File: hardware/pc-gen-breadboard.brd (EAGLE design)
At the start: 43.2 x 30.5 mm, 25 parts

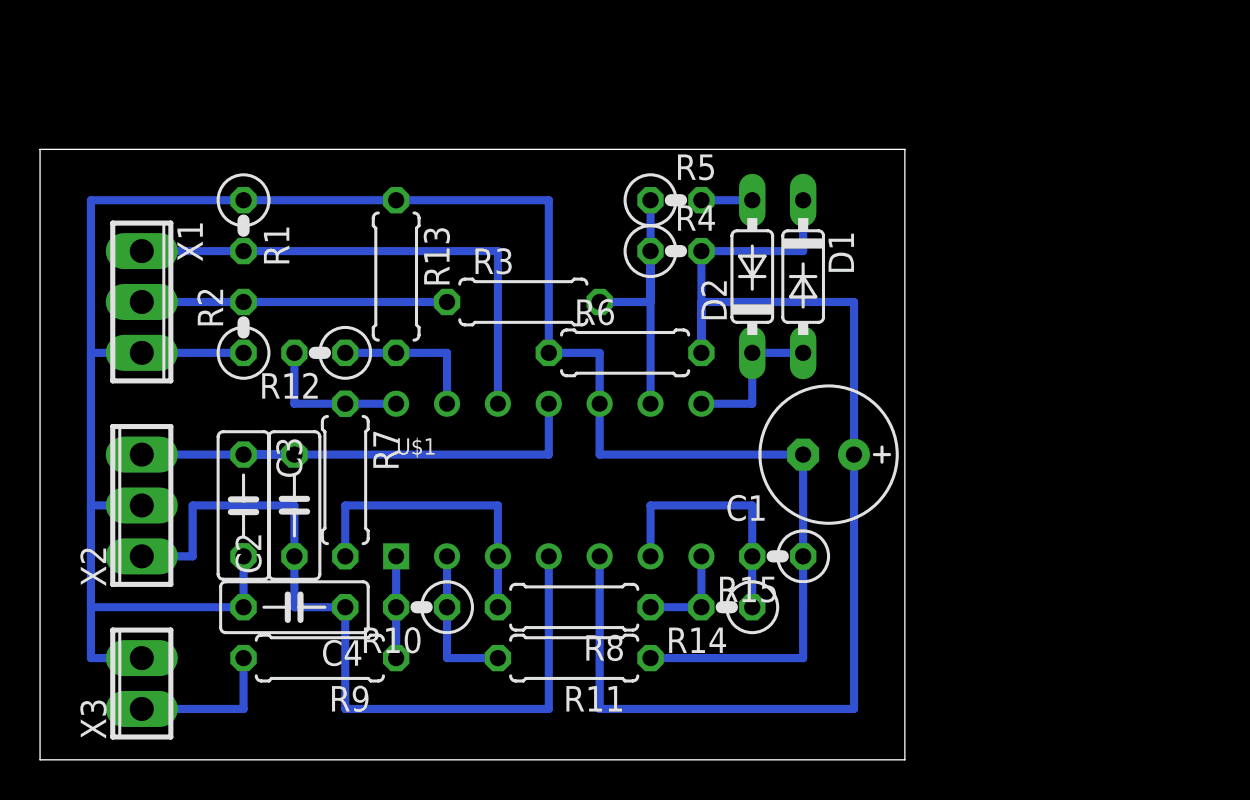
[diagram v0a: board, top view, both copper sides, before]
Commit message: gain selector added
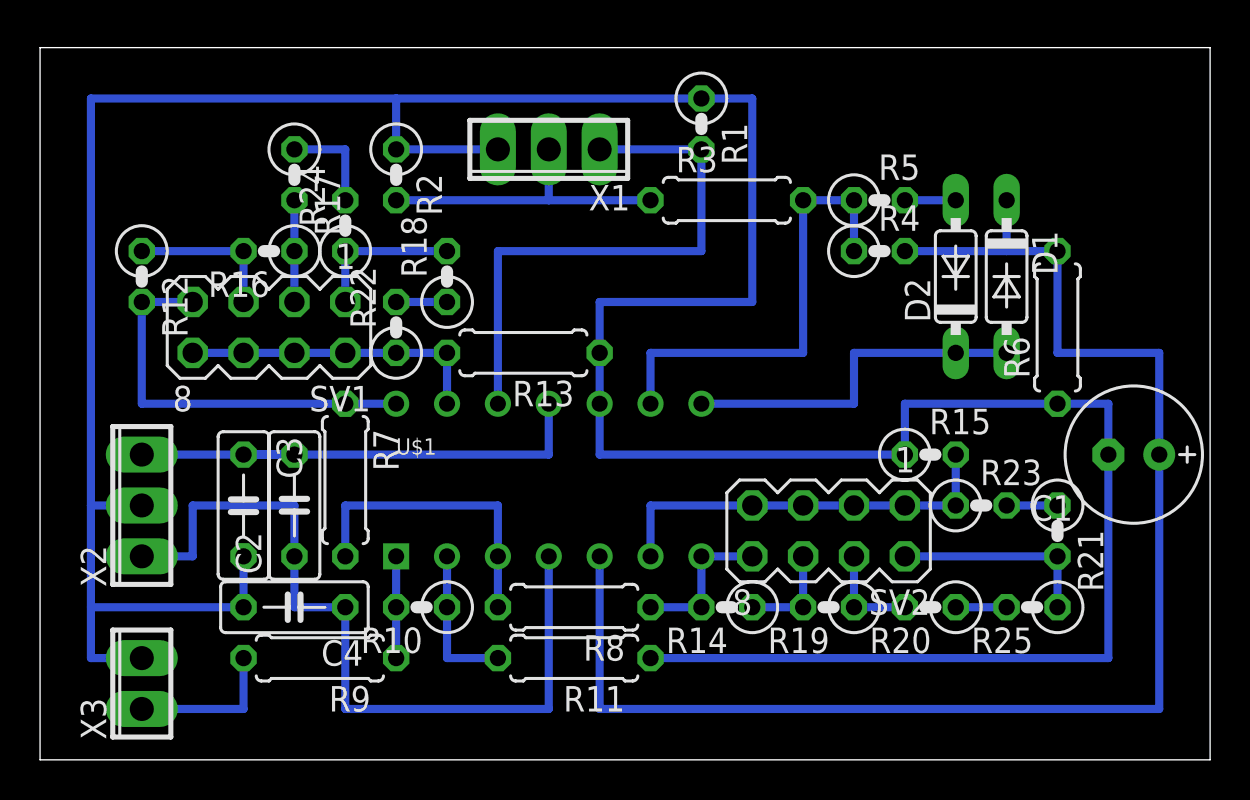
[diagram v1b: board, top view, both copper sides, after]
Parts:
- added R16, R19: 200k, rcl:0207/2V
- added R17, R20: 390k, rcl:0207/2V
- added R18, R21: 750k, rcl:0207/2V
- added R22, R23: 51k, rcl:0207/2V
- added R24, R25: 10k, rcl:0207/2V
- added SV1, SV2: (no value), con-lstb:MA04-2
- C1: value (none) -> 1u
- R6: value (none) -> 1k
- moved R1 23.4 mm to (33.0, 31.8)
- moved X1 21.7 mm to (25.4, 30.5), turned to 180 degrees
- moved R6 21.6 mm to (50.8, 21.6), turned to 90 degrees
- moved C1 15.2 mm to (54.6, 15.2)
- moved R3 11.4 mm to (34.3, 27.9)
- moved R2 10.8 mm to (17.8, 29.2), turned to 270 degrees
- moved D1 10.2 mm to (48.3, 24.1)
- moved D2 10.2 mm to (45.7, 24.1)
- moved R4 10.2 mm to (41.9, 25.4)
- moved R5 10.2 mm to (41.9, 27.9)
- moved R12 9.67 mm to (5.08, 24.1), turned to 270 degrees
- moved R15 9.16 mm to (44.5, 15.2), turned to 0 degrees
- moved R13 7.41 mm to (24.1, 20.3), turned to 180 degrees
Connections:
- new net N$17: R12.1, R16.2, SV1.5
- new net N$18: R16.1, R17.2, SV1.3
- new net N$19: R18.2, R24.1, SV1.1
- new net N$20: R14.1, R19.2, SV2.6
- new net N$21: R18.1, R22.2
- new net N$22: R13.2, R22.1, SV1.2, SV1.4, SV1.6, SV1.8, U$1.13
- new net N$23: R19.1, R20.2, SV2.4
- new net N$24: R17.1, R24.2
- new net N$25: R21.1, R23.2
- new net N$26: R20.1, R25.2
- net N$10: now also R23.1, SV2.1, SV2.3, SV2.5, SV2.7; no longer R14.1
- net N$12: now also SV2.8
- net N$5: now also R21.2, R25.1, SV2.2; no longer R12.1, R13.2, U$1.13
- net N$8: now also SV1.7
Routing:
- net GND: track 111.8 -> 172.7 mm
- net N$22: track 0.00 -> 15.2 mm
- net N$8: track 7.62 -> 20.3 mm
- net N$11: track 63.5 -> 73.7 mm
- net N$9: track 7.62 -> 17.8 mm
- net N$6: track 15.2 -> 22.9 mm
- net N$10: track 12.7 -> 20.3 mm
- net N$19: track 0.00 -> 7.62 mm
- net N$17: track 0.00 -> 7.62 mm
- net N$18: track 0.00 -> 5.08 mm
- net N$24: track 0.00 -> 5.08 mm
- net N$23: track 0.00 -> 5.08 mm
- net N$20: track 0.00 -> 5.08 mm
- net N$4: track 25.4 -> 27.9 mm
- net N$26: track 0.00 -> 2.54 mm
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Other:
- board size 43.2 x 30.5 mm -> 58.4 x 35.6 mm

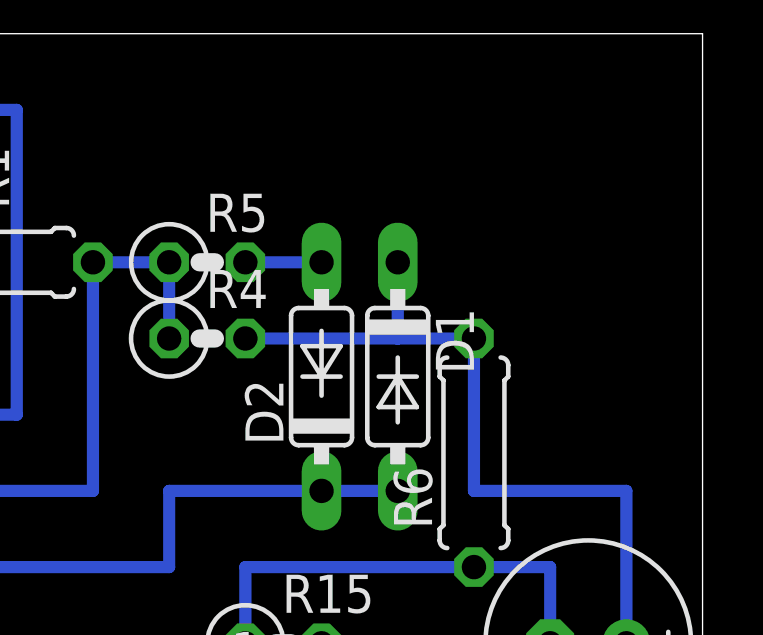
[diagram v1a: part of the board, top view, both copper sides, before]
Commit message: offest polarity selector added
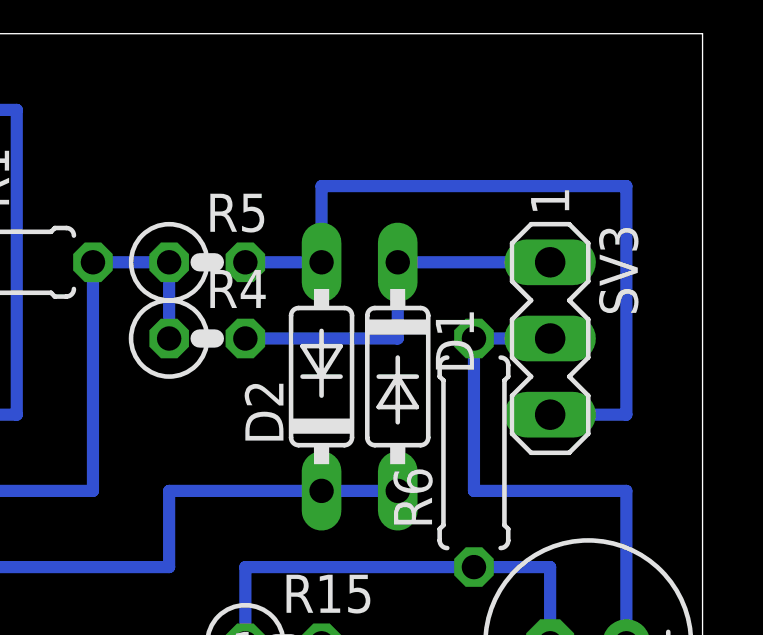
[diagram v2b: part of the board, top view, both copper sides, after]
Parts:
- added SV3: (no value), con-lstb:MA03-1
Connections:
- new net N$27: C1.+, R6.2, SV3.2, U$1.5
- net N$11: now also SV3.1; no longer C1.+, R6.2, U$1.5
- net N$7: now also SV3.3
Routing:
- net N$27: track 0.00 -> 66.0 mm
- net N$11: track 73.7 -> 12.7 mm
- net N$7: track 2.54 -> 25.4 mm
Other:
- board text added: "+"
- board text added: "-"
- board text added: "Polarity"
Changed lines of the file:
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@@
 <wire x1="58.42" y1="35.56" x2="0" y2="35.56" width="0" layer="20"/>
 <wire x1="0" y1="35.56" x2="0" y2="0" width="0" layer="20"/>
-<text x="-10.16" y="22.86" size="2.54" layer="49">In</text>
+<text x="22.86" y="40.64" size="2.54" layer="49">In</text>
 <text x="-10.16" y="2.54" size="2.54" layer="49">Out</text>
 <text x="-15.24" y="12.7" size="2.54" layer="49">Supply</text>
-<text x="-4.318" y="19.558" size="1.27" layer="49">GND</text>
-<text x="-4.318" y="22.098" size="1.27" layer="49">Offset</text>
-<text x="-4.318" y="24.892" size="1.27" layer="49">Signal</text>
+<text x="23.622" y="33.782" size="1.27" layer="49" rot="R90">GND</text>
+<text x="26.162" y="33.782" size="1.27" layer="49" rot="R90">Offset</text>
+<text x="28.448" y="33.782" size="1.27" layer="49" rot="R90">Signal</text>
 <text x="-3.81" y="12.192" size="1.27" layer="49">GND</text>
 <text x="-3.81" y="14.478" size="1.27" layer="49">+8V</text>
@@
 <text x="-4.064" y="4.572" size="1.27" layer="49">GND</text>
 <text x="-4.064" y="2.032" size="1.27" layer="49">Signal</text>
+<text x="60.96" y="24.13" size="2.54" layer="49">Polarity</text>
+<text x="59.182" y="25.908" size="1.27" layer="49">+</text>
+<text x="59.182" y="23.622" size="1.27" layer="49">-</text>
 </plain>
 <attributes>
@@
 <element name="R24" library="rcl" package="0207/2V" value="10k" x="15.24" y="26.67" rot="R90"/>
 <element name="R25" library="rcl" package="0207/2V" value="10k" x="49.53" y="7.62" rot="R180"/>
+<element name="SV3" library="con-lstb" package="MA03-1" value="" x="53.34" y="25.4" rot="R270">
+<attribute name="OC_NEWARK" value="unknown" x="53.34" y="25.4" size="1.27" layer="27" font="vector" ratio="20" rot="R270" display="off"/>
+<attribute name="MPN" value="" x="53.34" y="25.4" size="1.27" layer="27" font="vector" ratio="20" rot="R270" display="off"/>
+<attribute name="MF" value="" x="53.34" y="25.4" size="1.27" layer="27" font="vector" ratio="20" rot="R270" display="off"/>
+<attribute name="OC_FARNELL" value="unknown" x="53.34" y="25.4" size="1.27" layer="27" font="vector" ratio="20" rot="R270" display="off"/>
+</element>
 </elements>
 <signals>
@@
 <contactref element="D2" pad="A"/>
 <wire x1="43.18" y1="27.94" x2="45.72" y2="27.94" width="0.4064" layer="16"/>
+<contactref element="SV3" pad="3"/>
+<wire x1="53.34" y1="22.86" x2="55.88" y2="22.86" width="0.4064" layer="16"/>
+<wire x1="55.88" y1="22.86" x2="55.88" y2="30.48" width="0.4064" layer="16"/>
+<wire x1="55.88" y1="30.48" x2="45.72" y2="30.48" width="0.4064" layer="16"/>
+<wire x1="45.72" y1="30.48" x2="45.72" y2="27.94" width="0.4064" layer="16"/>
 </signal>
 <signal name="N$9">
@@
 </signal>
 <signal name="N$11">
+<contactref element="D1" pad="C"/>
+<wire x1="48.26" y1="27.94" x2="48.26" y2="25.4" width="0.4064" layer="16"/>
 <contactref element="R4" pad="2"/>
-<contactref element="D1" pad="C"/>
-<contactref element="C1" pad="+"/>
-<contactref element="R6" pad="2"/>
-<wire x1="48.26" y1="27.94" x2="48.26" y2="25.4" width="0.4064" layer="16"/>
-<wire x1="48.26" y1="25.4" x2="43.18" y2="25.4" width="0.4064" layer="16"/>
-<contactref element="U$1" pad="5"/>
-<wire x1="27.94" y1="10.16" x2="27.94" y2="2.54" width="0.4064" layer="16"/>
-<wire x1="27.94" y1="2.54" x2="55.88" y2="2.54" width="0.4064" layer="16"/>
-<wire x1="55.88" y1="2.54" x2="55.88" y2="15.24" width="0.4064" layer="16"/>
-<wire x1="55.88" y1="20.32" x2="55.88" y2="15.24" width="0.4064" layer="16"/>
-<wire x1="55.88" y1="20.32" x2="50.8" y2="20.32" width="0.4064" layer="16"/>
-<wire x1="50.8" y1="20.32" x2="50.8" y2="25.4" width="0.4064" layer="16"/>
-<wire x1="48.26" y1="25.4" x2="50.8" y2="25.4" width="0.4064" layer="16"/>
+<contactref element="SV3" pad="1"/>
+<wire x1="48.26" y1="27.94" x2="53.34" y2="27.94" width="0.4064" layer="16"/>
+<wire x1="43.18" y1="25.4" x2="48.26" y2="25.4" width="0.4064" layer="16"/>
 </signal>
 <signal name="N$12">
@@
 <wire x1="45.72" y1="7.62" x2="48.26" y2="7.62" width="0.4064" layer="16"/>
 </signal>
+<signal name="N$27">
+<contactref element="C1" pad="+"/>
+<contactref element="R6" pad="2"/>
+<contactref element="U$1" pad="5"/>
+<wire x1="27.94" y1="10.16" x2="27.94" y2="2.54" width="0.4064" layer="16"/>
+<wire x1="27.94" y1="2.54" x2="55.88" y2="2.54" width="0.4064" layer="16"/>
+<wire x1="55.88" y1="2.54" x2="55.88" y2="15.24" width="0.4064" layer="16"/>
+<wire x1="55.88" y1="20.32" x2="55.88" y2="15.24" width="0.4064" layer="16"/>
+<wire x1="55.88" y1="20.32" x2="50.8" y2="20.32" width="0.4064" layer="16"/>
+<wire x1="50.8" y1="20.32" x2="50.8" y2="25.4" width="0.4064" layer="16"/>
+<contactref element="SV3" pad="2"/>
+<wire x1="53.34" y1="25.4" x2="50.8" y2="25.4" width="0.4064" layer="16"/>
+</signal>
 </signals>

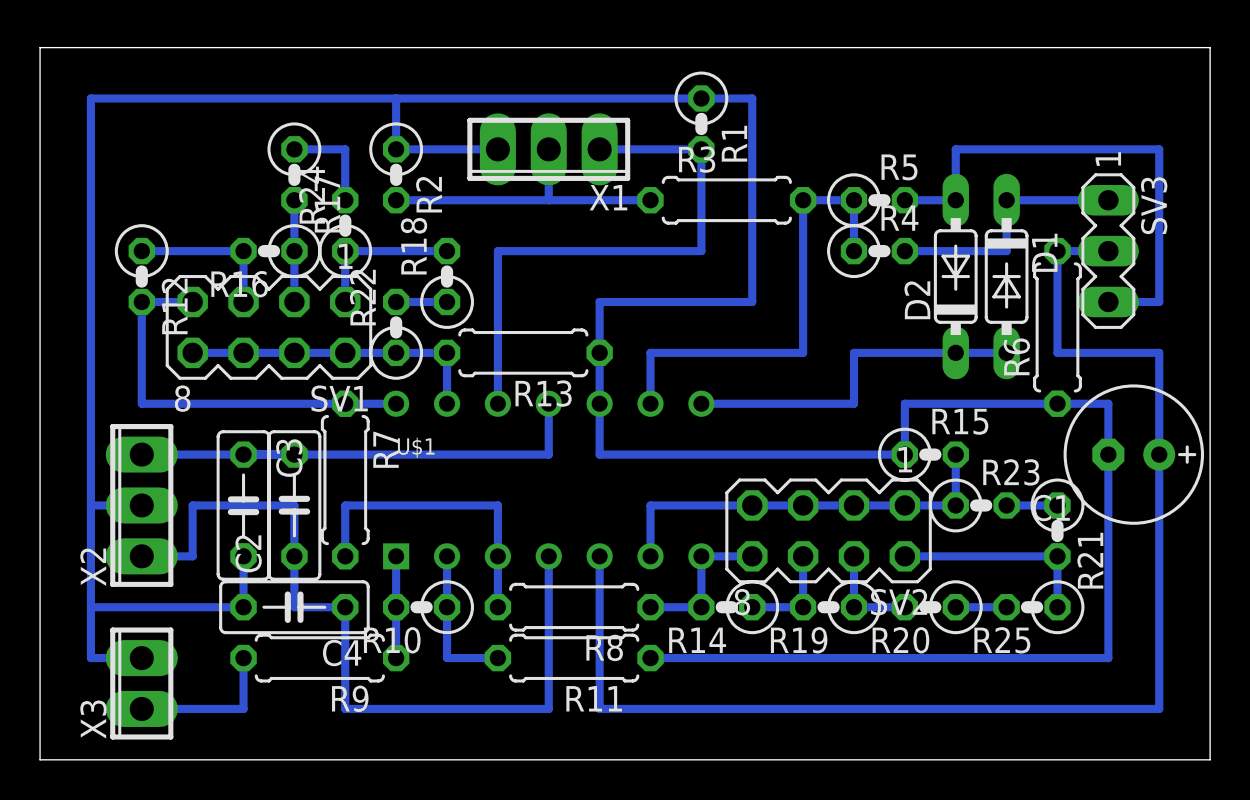
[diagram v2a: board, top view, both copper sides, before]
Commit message: small changes in layout to optimize pcb size
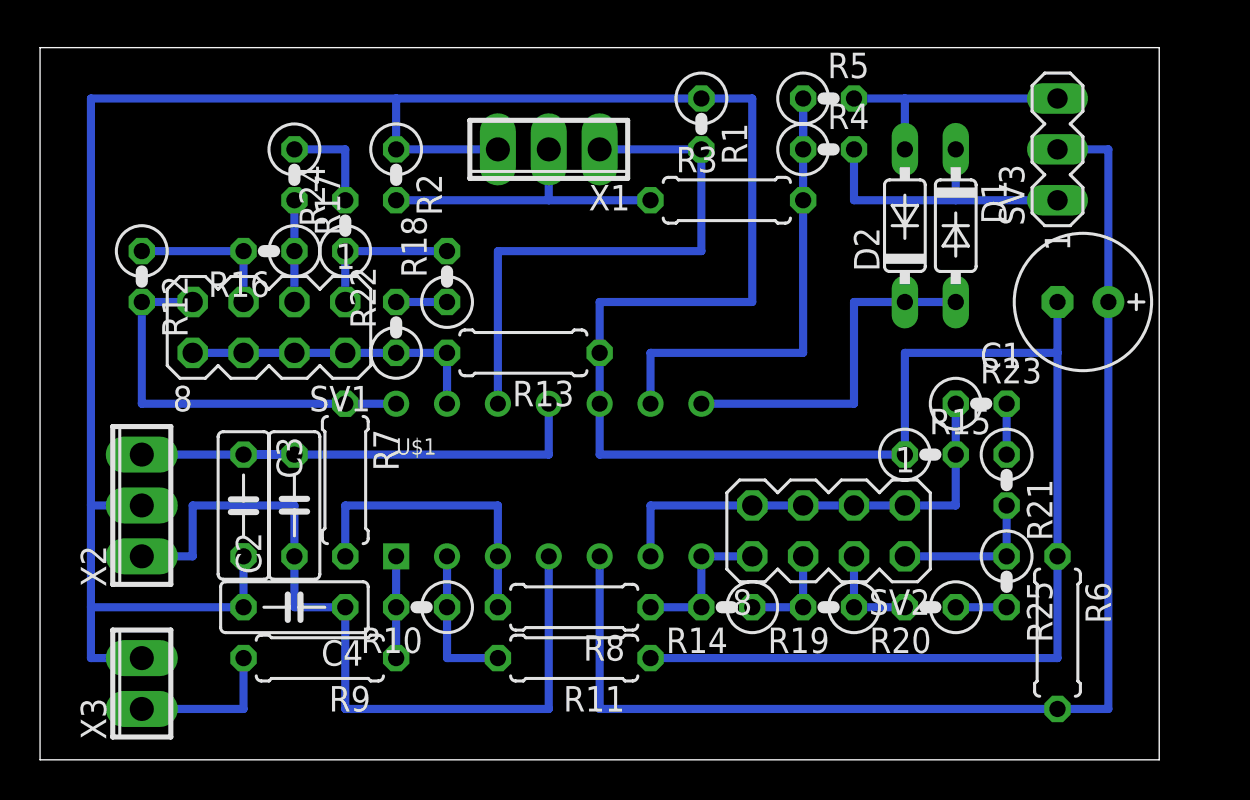
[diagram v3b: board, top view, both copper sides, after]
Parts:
- moved R6 15.2 mm to (50.8, 6.35), turned to 270 degrees
- moved C1 8.03 mm to (52.1, 22.9)
- moved SV3 5.68 mm to (50.8, 30.5), turned to 90 degrees
- moved R4 5.68 mm to (39.4, 30.5)
- moved R5 5.68 mm to (39.4, 33.0)
- moved R23 5.08 mm to (47.0, 17.8)
- moved D1 3.59 mm to (45.7, 26.7)
- moved D2 3.59 mm to (43.2, 26.7)
- moved R21 3.59 mm to (48.3, 14.0)
- moved R25 1.80 mm to (48.3, 8.89), turned to 270 degrees
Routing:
- net N$7: track 25.4 -> 12.7 mm
- net N$27: track 66.0 -> 63.5 mm
- net N$6: track 22.9 -> 25.4 mm
- net N$5: track 10.2 -> 7.62 mm
- net N$10: track 20.3 -> 22.9 mm
- net GND: track 172.7 -> 175.3 mm
- net N$11: track 12.7 -> 15.2 mm
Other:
- board size 58.4 x 35.6 mm -> 55.9 x 35.6 mm

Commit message: small changes in layout
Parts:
- R6: device rcl:0207/7 -> rcl:0207/2V
- moved R18 15.5 mm to (5.08, 26.7), turned to 270 degrees
- moved R22 14.5 mm to (6.35, 30.5), turned to 180 degrees
- moved D2 13.0 mm to (30.5, 29.2)
- moved R24 11.4 mm to (5.08, 21.6), turned to 270 degrees
- moved R3 11.4 mm to (24.1, 22.9)
- moved R1 10.9 mm to (24.1, 25.4), turned to 180 degrees
- moved R25 10.5 mm to (45.7, 19.1)
- moved R12 9.67 mm to (14.0, 20.3), turned to 0 degrees
- moved R14 9.67 mm to (43.2, 11.4), turned to 270 degrees
- moved R17 9.67 mm to (8.89, 20.3), turned to 0 degrees
- moved R15 9.16 mm to (36.8, 20.3)
- moved R23 9.16 mm to (39.4, 22.9)
- moved R21 9.16 mm to (43.2, 21.6)
- moved D1 8.98 mm to (36.8, 27.9), turned to 180 degrees
- moved R19 8.98 mm to (45.7, 14.0), turned to 270 degrees
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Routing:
- net GND: track 175.3 -> 162.6 mm
- net N$4: track 27.9 -> 15.2 mm
- net N$8: track 20.3 -> 7.62 mm
- net N$22: track 15.2 -> 25.4 mm
- net N$12: track 7.62 -> 17.8 mm
- net N$11: track 15.2 -> 7.62 mm
- net N$7: track 12.7 -> 17.8 mm
- net N$9: track 17.8 -> 12.7 mm
- net N$6: track 25.4 -> 30.5 mm
- net N$27: track 63.5 -> 61.0 mm
- net N$3: track 15.2 -> 17.8 mm
- net N$17: track 7.62 -> 5.08 mm
- net N$24: track 5.08 -> 2.54 mm
- net N$19: track 7.62 -> 5.08 mm
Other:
- board size 55.9 x 35.6 mm -> 53.3 x 35.6 mm
